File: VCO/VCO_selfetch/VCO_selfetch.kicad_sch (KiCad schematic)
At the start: 35 parts

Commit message: small fixes
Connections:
- net -12V: now also Q?.1 (C); no longer Q?.3 (E)
- net at Q?.2 (B), R?.2: now also Q?.3 (E); no longer Q?.1 (C)
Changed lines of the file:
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@@
     (pin "4")
   )
-  (symbol (lib_id "Transistor_BJT:BC558") (at 127 48.26 0) (unit 1)
+  (symbol (lib_id "Transistor_BJT:BC558") (at 127 48.26 0) (mirror x) (unit 1)
     (in_bom yes) (on_board yes) (fields_autoplaced)
-    (property "Reference" "Q?" (id 0) (at 132.08 46.9899 0)
+    (property "Reference" "Q?" (id 0) (at 131.8514 47.4253 0)
       (effects (font (size 1.27 1.27)) (justify left))
     )
-    (property "Value" "BC558" (id 1) (at 132.08 49.5299 0)
+    (property "Value" "BC558" (id 1) (at 131.8514 49.9622 0)
       (effects (font (size 1.27 1.27)) (justify left))
     )
-    (property "Footprint" "Package_TO_SOT_THT:TO-92_Inline" (id 2) (at 132.08 50.165 0)
+    (property "Footprint" "Package_TO_SOT_THT:TO-92_Inline" (id 2) (at 132.08 46.355 0)
       (effects (font (size 1.27 1.27) italic) (justify left) hide)
     )

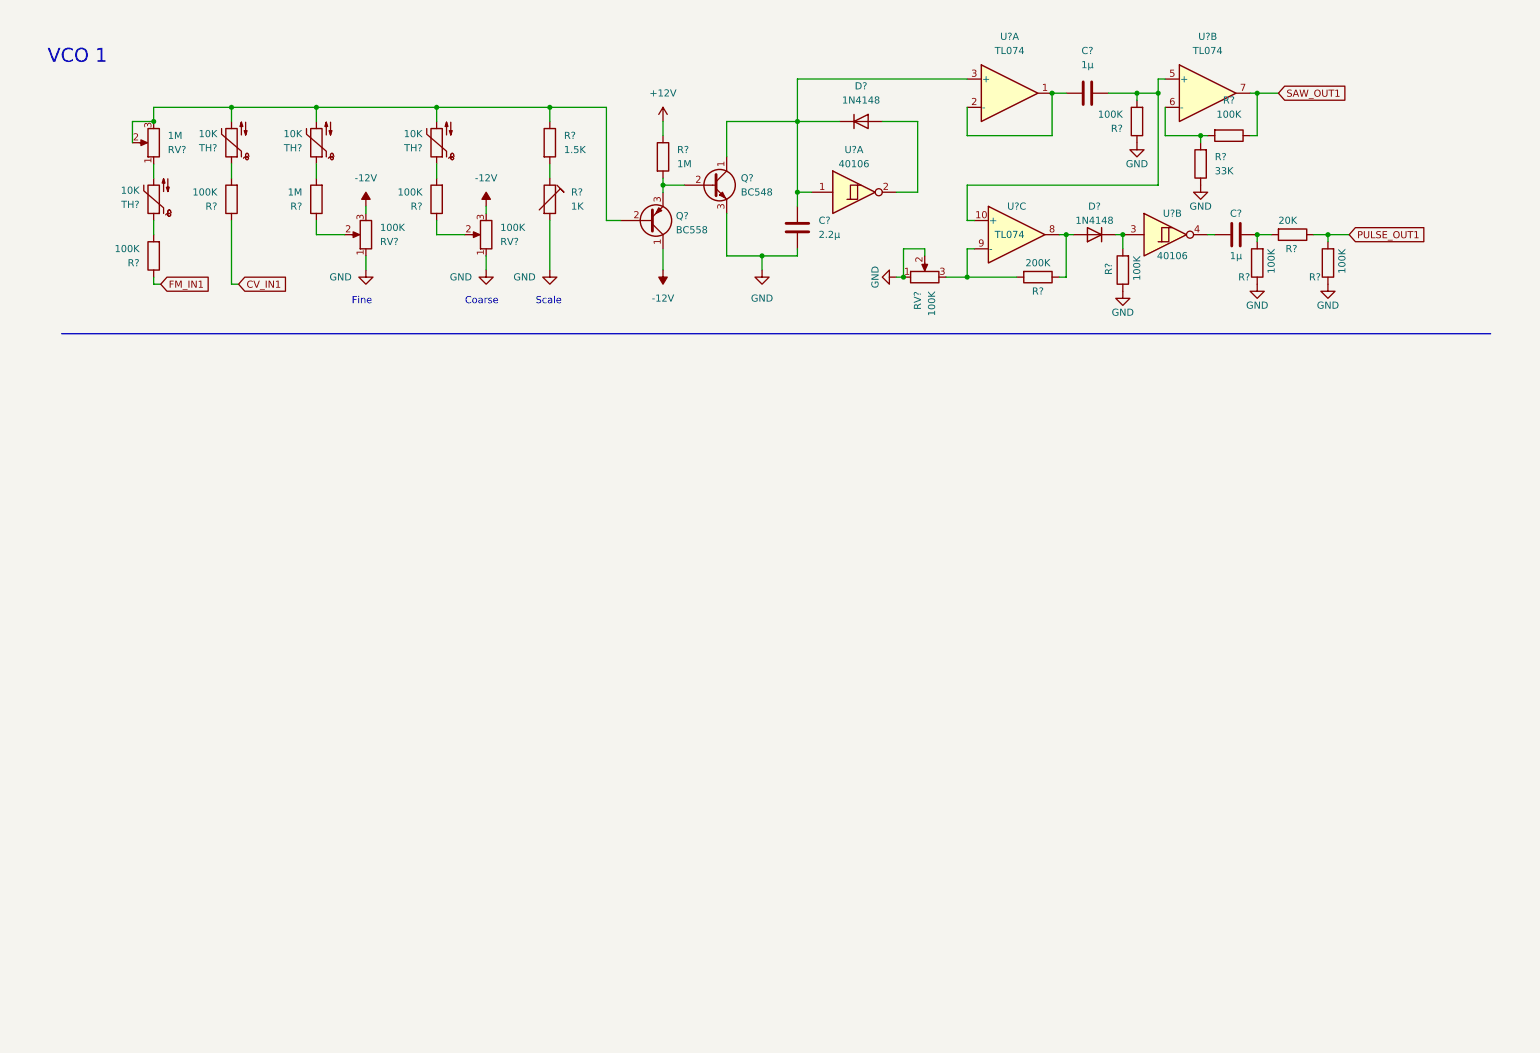
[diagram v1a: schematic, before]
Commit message: changes vco
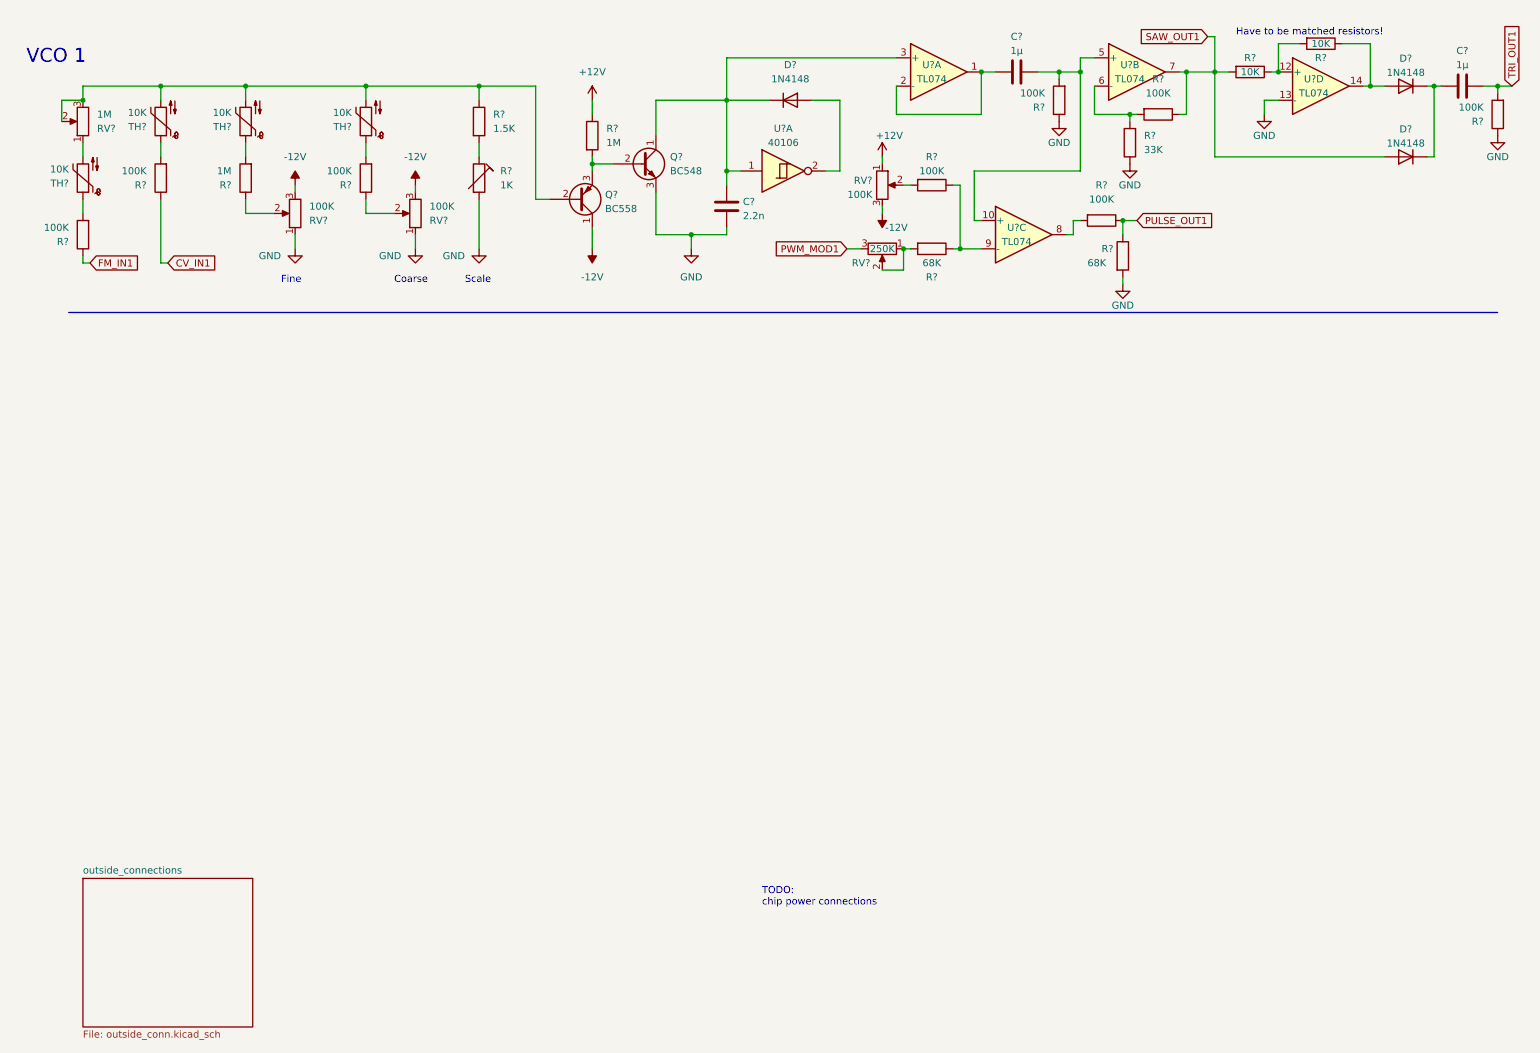
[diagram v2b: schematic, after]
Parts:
- removed C?: 1µ, symbol Device:C
- removed D?: 1N4148, Diode_THT:D_DO-35_SOD27_P7.62mm_Horizontal, symbol Diode:1N4148
- removed R? (x3): 100K, symbol Device:R
- removed R?: 200K, symbol Device:R
- removed R?: 20K, symbol Device:R
- removed RV?: 100K, symbol Device:R_Potentiometer
- removed U?: 40106, symbol 4xxx:40106
- removed U?: TL074, symbol Amplifier_Operational:TL074
- added C?: 1µ, symbol Device:C
- added D? (x2): 1N4148, Diode_THT:D_DO-35_SOD27_P7.62mm_Horizontal, symbol Diode:1N4148
- added R? (x2): 68K, symbol Device:R
- added R? (x3): 100K, symbol Device:R
- added R? (x2): 10K, symbol Device:R
- added RV?: 100K, symbol Device:R_Potentiometer
- added RV?: 250K, symbol Device:R_Potentiometer
- added U? (x2): TL074, symbol Amplifier_Operational:TL074
- C?: value 2.2µ -> 2.2n
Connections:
- net +12V: now also RV?.1
- net -12V: now also RV?.3
- net GND: now also R?.1, R?.2, U?.13 (-)
- net PULSE_OUT1: now also R?.1, R?.1
- net SAW_OUT1: now also D?.2 (A), R?.2
- net at C?.1, R?.2, U?.5 (+): now also U?.10 (+)
- new net: R?.1, R?.1, U?.9 (-)
- new net: R?.2, RV?.1, RV?.2
- new net: D?.2 (A), R?.1, U?.14
- new net: R?.1, R?.2, U?.12 (+)
- new net: R?.2, RV?.2
- new net: R?.2, U?.8
- new net: C?.2, D?.1 (K), D?.1 (K)
- new net PWM_MOD1: RV?.3
- new net TRI_OUT1: C?.1, R?.2
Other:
- added sheet outside_connections (outside_conn.kicad_sch)
- note added: "Have to be matched resistors!"
- note added: "TODO: chip power connections"
- moved on the sheet: C?, D?, Q?, R?, RV?, TH?, U?A, U?B

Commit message: added vco 2 and 3
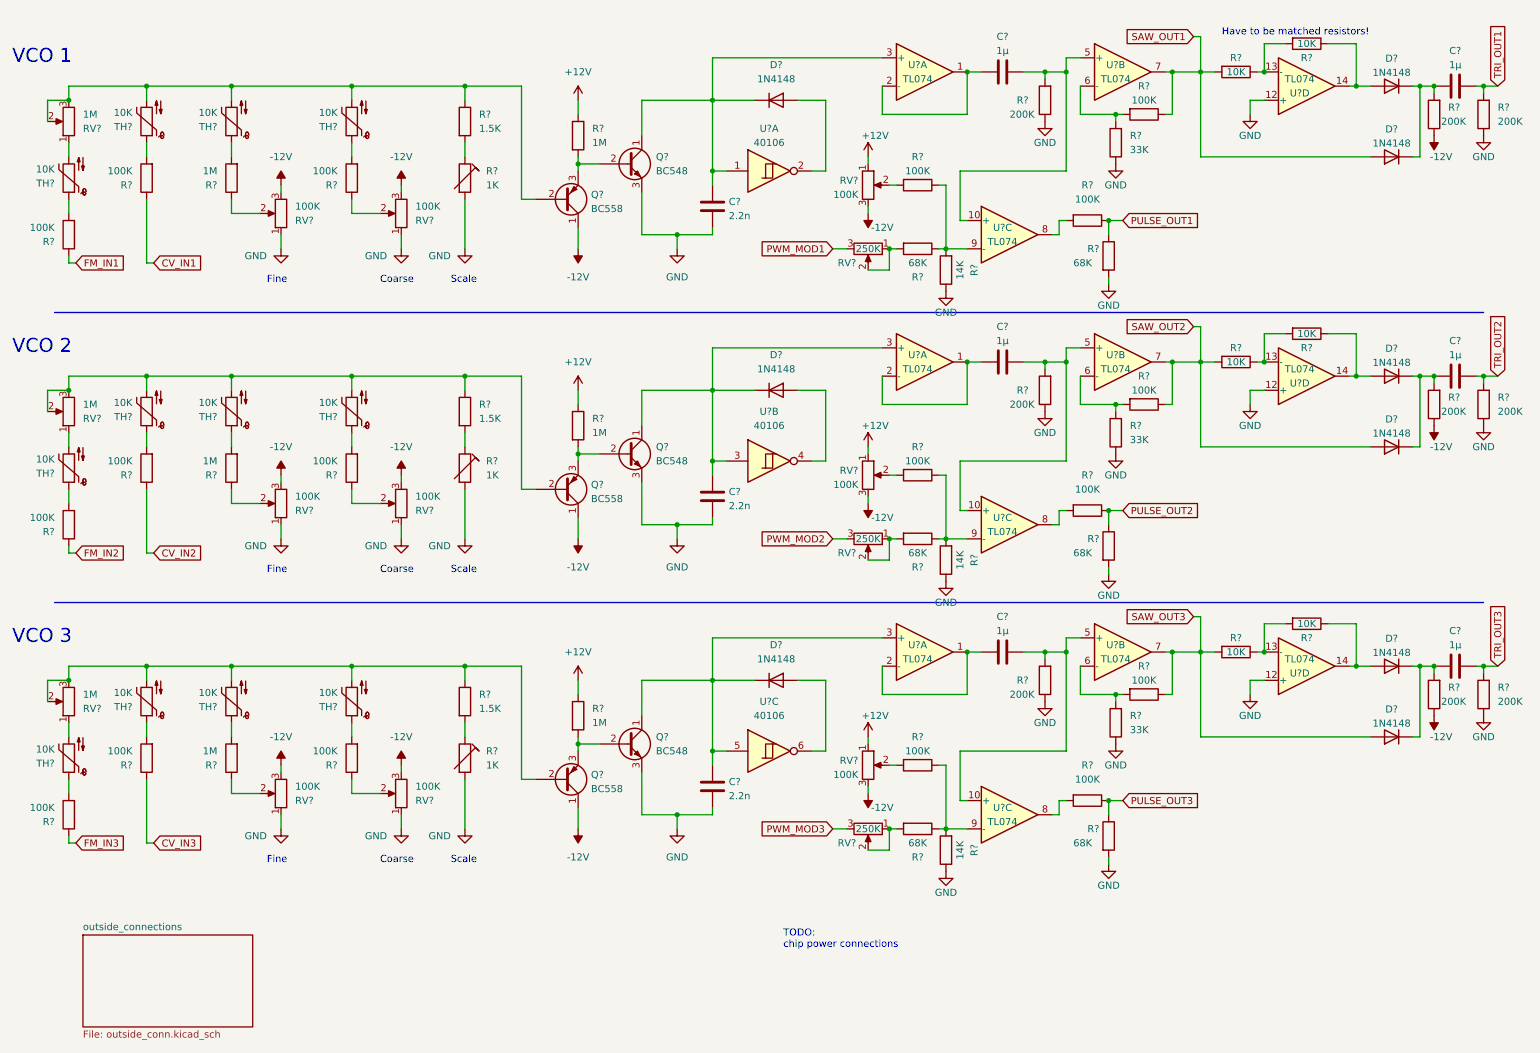
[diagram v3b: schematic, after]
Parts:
- added C? (x4): 1µ, symbol Device:C
- added C? (x2): 2.2n, symbol Device:C
- added D? (x6): 1N4148, Diode_THT:D_DO-35_SOD27_P7.62mm_Horizontal, symbol Diode:1N4148
- added Q? (x2): BC548, Package_TO_SOT_THT:TO-92_Inline, symbol Transistor_BJT:BC548
- added Q? (x2): BC558, Package_TO_SOT_THT:TO-92_Inline, symbol Transistor_BJT:BC558
- added R? (x7): 200K, symbol Device:R
- added R? (x2): 33K, symbol Device:R
- added R? (x12): 100K, symbol Device:R
- added R? (x3): 14K, symbol Device:R
- added R? (x2): 1K, symbol Device:R_Trim
- added R? (x4): 10K, symbol Device:R
- added R? (x4): 68K, symbol Device:R
- added R? (x2): 1.5K, symbol Device:R
- added R? (x4): 1M, symbol Device:R
- added RV? (x6): 100K, symbol Device:R_Potentiometer
- added RV? (x2): 1M, symbol Device:R_Potentiometer
- added RV? (x2): 250K, symbol Device:R_Potentiometer
- added TH? (x8): 10K, symbol Device:Thermistor_NTC
- added U? (x8): TL074, symbol Amplifier_Operational:TL074
- added U? (x2): 40106, symbol 4xxx:40106
- R? (x2): value 100K -> 200K
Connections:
- net +12V: now also R?.1, R?.1, RV?.1, RV?.1
- net -12V: now also Q?.1 (C), Q?.1 (C), R?.1, R?.1, R?.1, RV?.3, RV?.3, RV?.3, RV?.3, RV?.3, RV?.3
- net GND: now also U?.12 (+), C?.1, C?.1, Q?.3 (E), Q?.3 (E), R?.1, R?.1, R?.1, R?.1, R?.1, R?.1, R?.1, R?.1, R?.1, R?.2, R?.2, R?.2, R?.2, RV?.1, RV?.1, RV?.1, RV?.1, U?.12 (+), U?.12 (+); no longer U?.13 (-)
- net at R?.1, R?.1, U?.9 (-): now also R?.2
- net at R?.1, R?.2: now also U?.13 (-); no longer U?.12 (+)
- net at C?.2, D?.1 (K), D?.1 (K): now also R?.2
- new net: C?.2, D?.1 (K), D?.1 (K), R?.2 (x2)
- new net: R?.1, RV?.2 (x4)
- new net: R?.2, R?.2, U?.6 (-) (x2)
- new net: R?.2, TH?.1 (x8)
- new net: Q?.2 (B), R?.1, RV?.2, RV?.3, TH?.2, TH?.2, TH?.2 (x2)
- new net: C?.2, D?.1 (K), Q?.1 (C), U?.3, U?.3 (+)
- new net: Q?.2 (B), Q?.3 (E), R?.2 (x2)
- new net: R?.2, U?.8 (x2)
- new net: RV?.1, TH?.2 (x2)
- new net: C?.2, U?.1, U?.2 (-) (x2)
- new net: C?.2, D?.1 (K), Q?.1 (C), U?.3 (+), U?.5
- new net: R?.1, R?.2, U?.13 (-) (x2)
- new net: D?.2 (A), R?.1, U?.14 (x2)
- new net: C?.1, R?.2, U?.10 (+), U?.5 (+) (x2)
- new net: R?.1, R?.2 (x2)
- new net: R?.1, R?.1, R?.2, U?.9 (-) (x2)
- new net: D?.2 (A), U?.6
- new net: D?.2 (A), U?.4
- new net: R?.2, RV?.1, RV?.2 (x2)
- new net: R?.2, RV?.2 (x2)
- new net CV_IN2: R?.1
- new net CV_IN3: R?.1
- new net FM_IN2: R?.1
- new net FM_IN3: R?.1
- new net PULSE_OUT2: R?.1, R?.1
- new net PULSE_OUT3: R?.1, R?.1
- new net PWM_MOD2: RV?.3
- new net PWM_MOD3: RV?.3
- new net SAW_OUT2: D?.2 (A), R?.1, R?.2, U?.7
- new net SAW_OUT3: D?.2 (A), R?.1, R?.2, U?.7
- new net TRI_OUT2: C?.1, R?.2
- new net TRI_OUT3: C?.1, R?.2
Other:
- note added: "VCO 2"
- note added: "VCO 3"
- moved on the sheet: C?, D?, Q?, R?, RV?, TH?, U?A, U?B, U?C, U?D

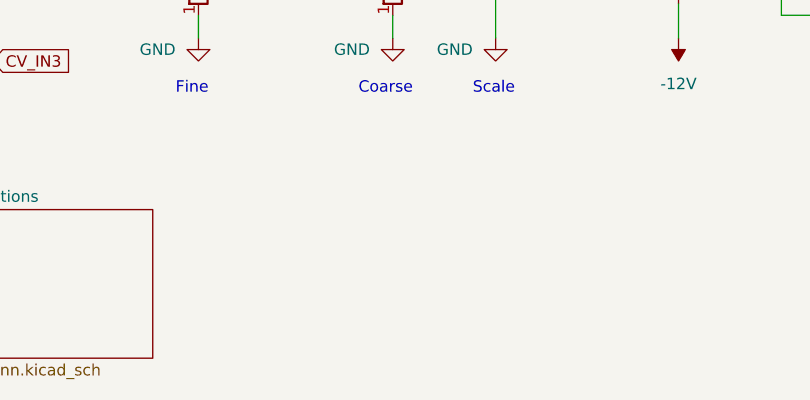
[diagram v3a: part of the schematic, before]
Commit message: simple vco's added
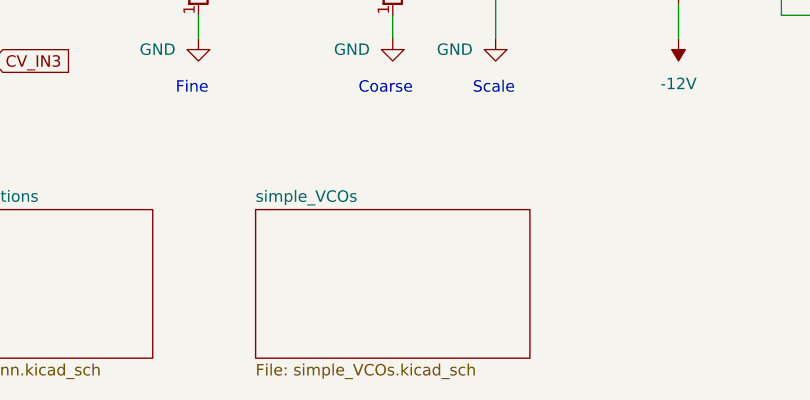
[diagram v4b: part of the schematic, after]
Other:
- added sheet simple_VCOs (simple_VCOs.kicad_sch)

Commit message: continue
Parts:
- gave numbers to parts that had none: 112
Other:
- added sheet power (power.kicad_sch)

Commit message: footprint WIP
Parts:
- removed Q13, Q14, Q15: BC558, Package_TO_SOT_THT:TO-92_Inline, symbol Transistor_BJT:BC558
- removed Q16, Q17, Q18: BC548, Package_TO_SOT_THT:TO-92_Inline, symbol Transistor_BJT:BC548
- added Q13, Q14, Q25: BC858, Package_TO_SOT_SMD:SOT-23, symbol Transistor_BJT:BC858
- added Q15, Q16, Q26: BC848, Package_TO_SOT_SMD:SOT-23, symbol Transistor_BJT:BC848
- C10, C11, C12, C13, C14, C15, C7, C8, C9: footprint (none) -> Capacitor_SMD:C_0402_1005Metric_Pad0.74x0.62mm_HandSolder
- D10, D11, D12, D13, D14, D15, D7, D8, D9: footprint Diode_THT:D_DO-35_SOD27_P7.62mm_Horizontal -> Diode_SMD:D_SOD-123
- R37, R38, R39, R40, R41, R42, R43, R44, R45, R46, R47, R48, R49, R51, R53, R55, R56, R57, R58, R59, R60, R61, R62, R63, R64, R65, R66, R67, R68, R69, R70, R71, R72, R73, R74, R75, R76, R77, R78, R79, R80, R81, R82, R83, R84, R85, R86, R87, R88, R89, R90, R91, R92, R93, TH1, TH10, TH11, TH12, TH2, TH3, TH4, TH5, TH6, TH7, TH8, TH9: footprint (none) -> Resistor_SMD:R_0603_1608Metric_Pad0.98x0.95mm_HandSolder
- R50, R52, R54: footprint (none) -> Potentiometer_THT:Potentiometer_Bourns_3296W_Vertical
- RV1, RV10, RV11, RV12, RV13, RV14, RV15, RV2, RV3, RV4, RV5, RV6, RV7, RV8, RV9: footprint (none) -> Connector_PinHeader_2.54mm:PinHeader_1x03_P2.54mm_Vertical
- U1, U2, U3, U4: footprint (none) -> Package_DIP:DIP-14_W7.62mm_Socket
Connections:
- net -12V: now also Q13.3 (C), Q14.3 (C), Q25.3 (C)
- net GND: now also Q15.2 (E), Q16.2 (E), Q26.2 (E)
- net at R53.1, RV3.2, RV3.3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: now also Q14.1 (B)
- net at C8.2, D8.1 (K), U1.3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: now also Q15.3 (C)
- net at R56.2: now also Q13.2 (E), Q15.1 (B)
- net at R57.2: now also Q14.2 (E), Q16.1 (B)
- net at R49.1, RV1.2, RV1.3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: now also Q25.1 (B)
- net at R51.1, RV2.2, RV2.3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: now also Q13.1 (B)
- net at C9.2, D9.1 (K), U1.5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: now also Q16.3 (C)
- net at C7.2, D7.1 (K), U1.1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: now also Q26.3 (C)
- net at R55.2: now also Q25.2 (E), Q26.1 (B)
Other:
- note added: "Originally BC558 and BC548 pairs, BC559 and BC549 also option for TO92"
- note removed: "TODO: chip power connections"

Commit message: all save
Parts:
- added J10: FM_in_3, Connector_PinHeader_2.54mm:PinHeader_1x02_P2.54mm_Vertical, symbol Connector:Conn_01x02_Pin
- added J11: CV_in_1, Connector_PinHeader_2.54mm:PinHeader_1x02_P2.54mm_Vertical, symbol Connector:Conn_01x02_Pin
- added J12: CV_in_2, Connector_PinHeader_2.54mm:PinHeader_1x02_P2.54mm_Vertical, symbol Connector:Conn_01x02_Pin
- added J13: CV_in_3, Connector_PinHeader_2.54mm:PinHeader_1x02_P2.54mm_Vertical, symbol Connector:Conn_01x02_Pin
- added J14: PWMMOD_in_1, Connector_PinHeader_2.54mm:PinHeader_1x02_P2.54mm_Vertical, symbol Connector:Conn_01x02_Pin
- added J15: PWMMOD_in_2, Connector_PinHeader_2.54mm:PinHeader_1x02_P2.54mm_Vertical, symbol Connector:Conn_01x02_Pin
- added J16: PWMMOD_IN_3, Connector_PinHeader_2.54mm:PinHeader_1x02_P2.54mm_Vertical, symbol Connector:Conn_01x02_Pin
- added J6: FM_in_1, Connector_PinHeader_2.54mm:PinHeader_1x02_P2.54mm_Vertical, symbol Connector:Conn_01x02_Pin
- added J9: FM_in_2, Connector_PinHeader_2.54mm:PinHeader_1x02_P2.54mm_Vertical, symbol Connector:Conn_01x02_Pin
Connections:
- net CV_IN1: now also J11.1 (Pin_1)
- net CV_IN2: now also J12.1 (Pin_1)
- net CV_IN3: now also J13.1 (Pin_1)
- net FM_IN1: now also J6.1 (Pin_1)
- net FM_IN2: now also J9.1 (Pin_1)
- net FM_IN3: now also J10.1 (Pin_1)
- net GND: now also J10.2 (Pin_2), J11.2 (Pin_2), J12.2 (Pin_2), J13.2 (Pin_2), J14.2 (Pin_2), J15.2 (Pin_2), J16.2 (Pin_2), J6.2 (Pin_2), J9.2 (Pin_2)
- net PWM_MOD1: now also J14.1 (Pin_1)
- net PWM_MOD2: now also J15.1 (Pin_1)
- net PWM_MOD3: now also J16.1 (Pin_1)
